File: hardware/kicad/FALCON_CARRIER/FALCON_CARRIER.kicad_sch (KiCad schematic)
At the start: 37 parts, among them J1 POWER_INPUT, J10 LEAK_SENSOR_TBD, J11 FAN_TBD, J12 SERVICE_I2C, J2 BAR02_I2C, J3 GPS_UART, J4 INA260_BAT_LOGIC, J5 INA260_SOLAR_0X41, J6 MCP9808_0X18, J7 ANEMOMETER, J8 WIND_VANE, J9 DS18B20_OPTION, U1 REGULATOR_3V3_TBD, U2 ESP32_DEVKITC_V4_WROOM32E, U3 BNO085_SPI, U4 ADS1115_0X48, U5 FAN_DRIVER_TBD

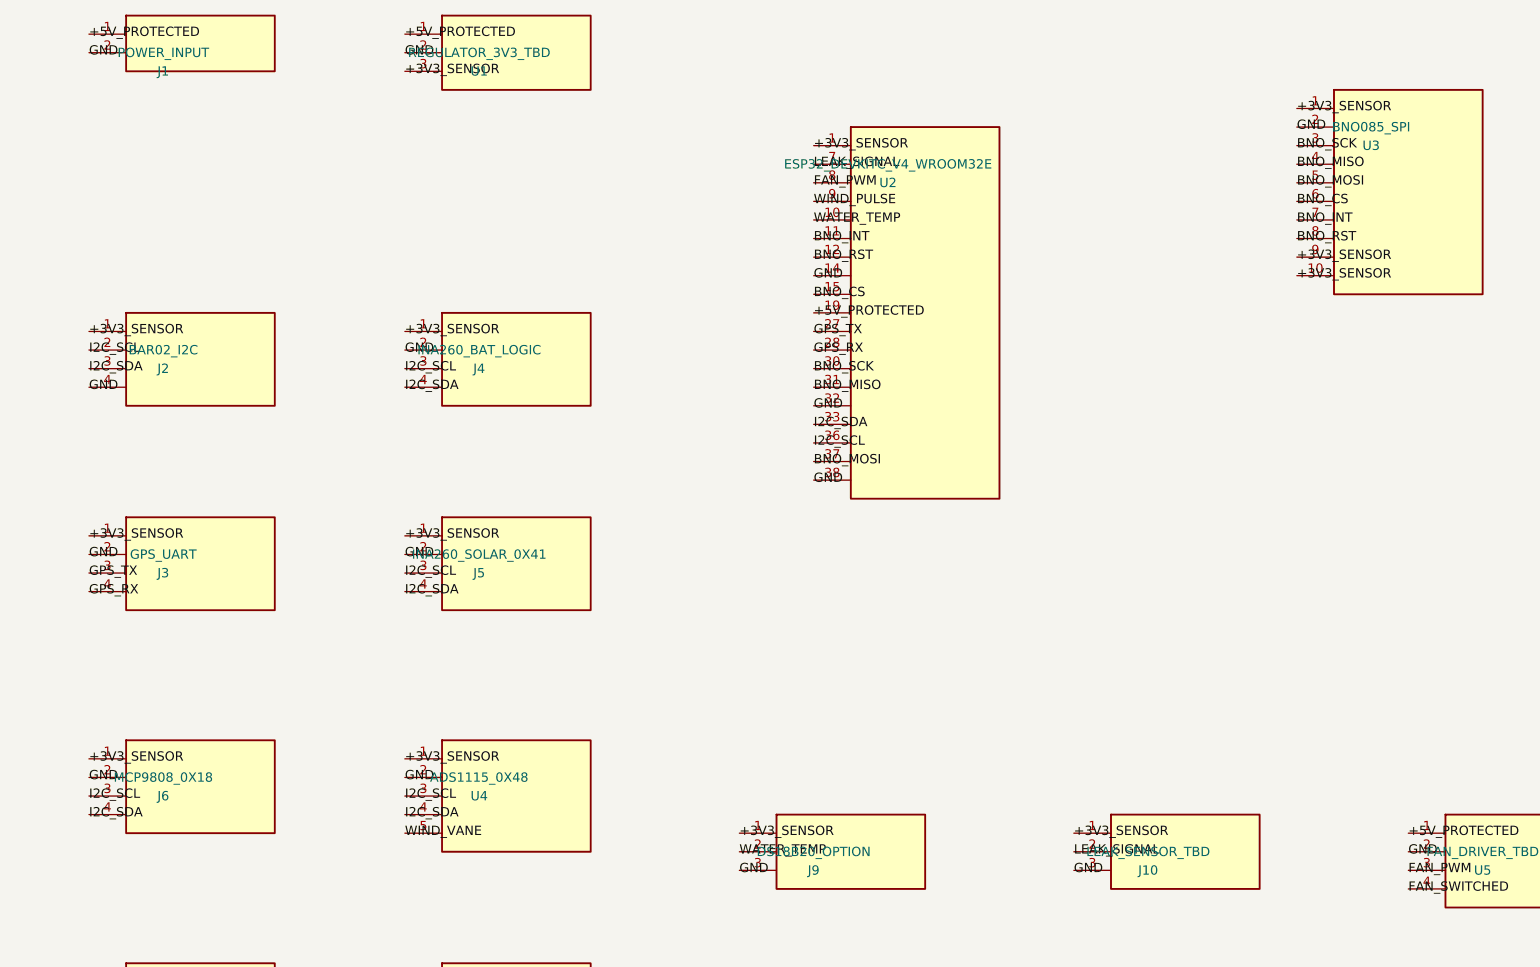
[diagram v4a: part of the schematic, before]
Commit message: Replace provisional carrier modules with official CAD footprints
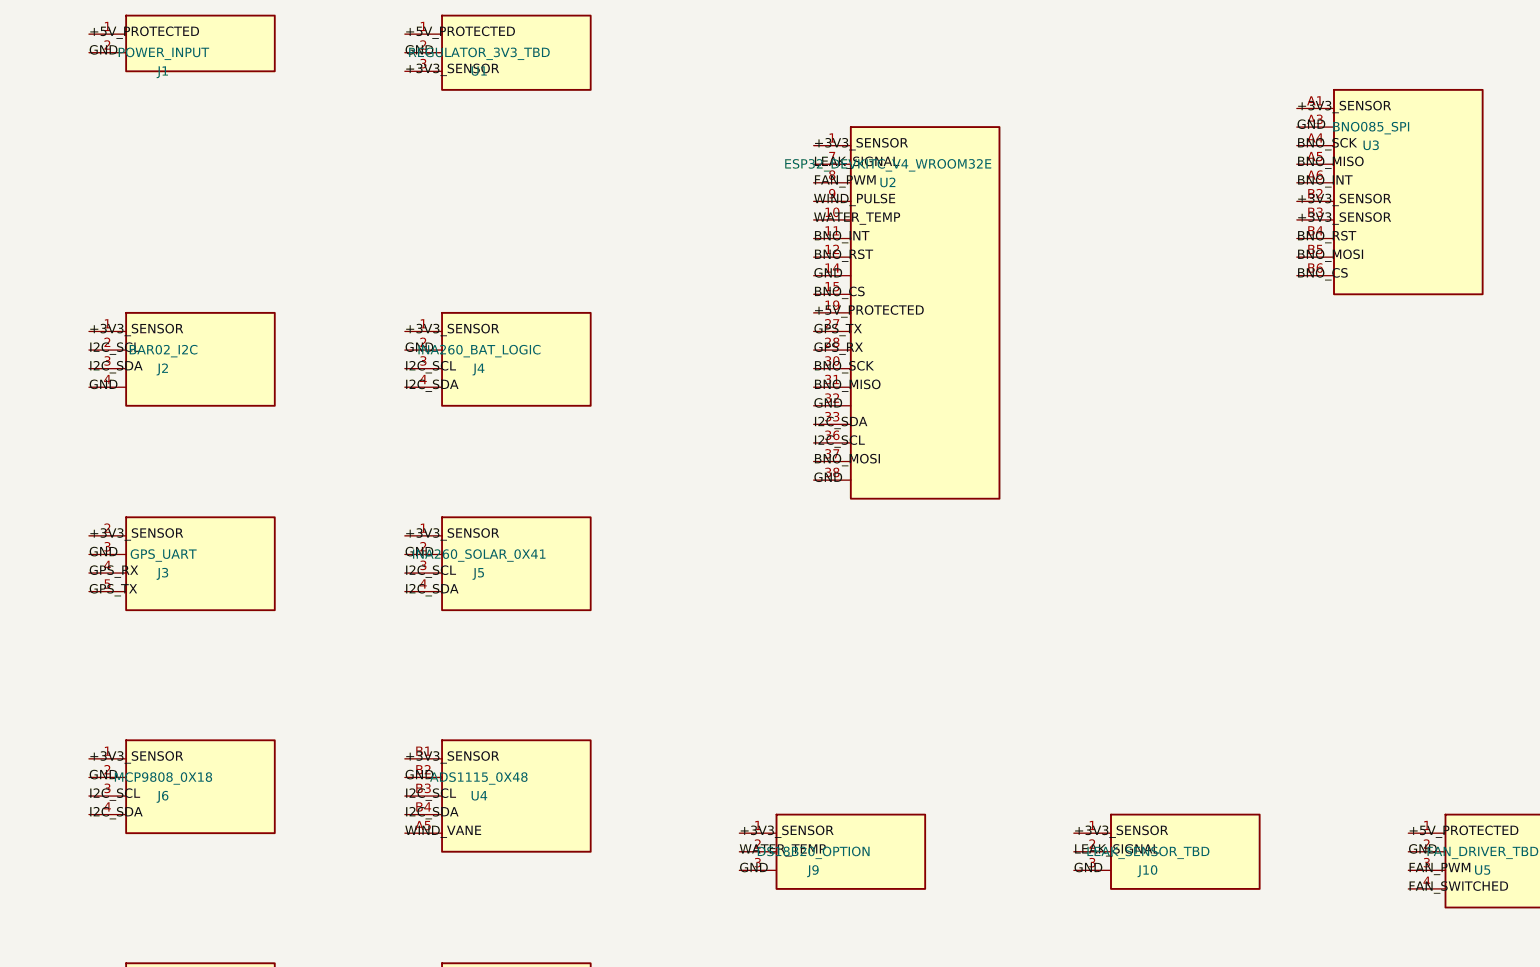
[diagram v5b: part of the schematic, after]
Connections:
- net +3V3_SENSOR: now also J3.2 (+3V3_SENSOR), U3.A1 (+3V3_SENSOR), U3.B2 (+3V3_SENSOR), U3.B3 (+3V3_SENSOR), U4.B1 (+3V3_SENSOR); no longer J3.1 (+3V3_SENSOR), U3.1 (+3V3_SENSOR), U3.10 (+3V3_SENSOR), U3.9 (+3V3_SENSOR), U4.1 (+3V3_SENSOR)
- net BNO_CS: now also U3.B6 (BNO_CS); no longer U3.6 (BNO_CS)
- net BNO_INT: now also U3.A6 (BNO_INT); no longer U3.7 (BNO_INT)
- net BNO_MISO: now also U3.A5 (BNO_MISO); no longer U3.4 (BNO_MISO)
- net BNO_MOSI: now also U3.B5 (BNO_MOSI); no longer U3.5 (BNO_MOSI)
- net BNO_RST: now also U3.B4 (BNO_RST); no longer U3.8 (BNO_RST)
- net BNO_SCK: now also U3.A4 (BNO_SCK); no longer U3.3 (BNO_SCK)
- net GND: now also J3.3 (GND), U3.A3 (GND), U4.B2 (GND); no longer J3.2 (GND), U3.2 (GND), U4.2 (GND)
- net GPS_TX: now also J3.5 (GPS_TX); no longer J3.3 (GPS_TX)
- net I2C_SCL: now also U4.B3 (I2C_SCL); no longer U4.3 (I2C_SCL)
- net I2C_SDA: now also U4.B4 (I2C_SDA); no longer U4.4 (I2C_SDA)
- net WIND_VANE: now also U4.A5 (WIND_VANE); no longer U4.5 (WIND_VANE)
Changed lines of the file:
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@@
   (label "BNO_MISO" (at 210.82 53.34 0)
     (effects (font (size 1.27 1.27))))
-  (label "BNO_MOSI" (at 210.82 55.88 0)
-    (effects (font (size 1.27 1.27))))
-  (label "BNO_CS" (at 210.82 58.42 0)
-    (effects (font (size 1.27 1.27))))
-  (label "BNO_INT" (at 210.82 60.96 0)
+  (label "BNO_INT" (at 210.82 55.88 0)
+    (effects (font (size 1.27 1.27))))
+  (label "+3V3_SENSOR" (at 210.82 58.42 0)
+    (effects (font (size 1.27 1.27))))
+  (label "+3V3_SENSOR" (at 210.82 60.96 0)
     (effects (font (size 1.27 1.27))))
   (label "BNO_RST" (at 210.82 63.50 0)
     (effects (font (size 1.27 1.27))))
-  (label "+3V3_SENSOR" (at 210.82 66.04 0)
-    (effects (font (size 1.27 1.27))))
-  (label "+3V3_SENSOR" (at 210.82 68.58 0)
+  (label "BNO_MOSI" (at 210.82 66.04 0)
+    (effects (font (size 1.27 1.27))))
+  (label "BNO_CS" (at 210.82 68.58 0)
     (effects (font (size 1.27 1.27))))
   (label "+3V3_SENSOR" (at 45.72 76.20 0)
@@
   (label "GND" (at 45.72 106.68 0)
     (effects (font (size 1.27 1.27))))
-  (label "GPS_TX" (at 45.72 109.22 0)
-    (effects (font (size 1.27 1.27))))
-  (label "GPS_RX" (at 45.72 111.76 0)
+  (label "GPS_RX" (at 45.72 109.22 0)
+    (effects (font (size 1.27 1.27))))
+  (label "GPS_TX" (at 45.72 111.76 0)
     (effects (font (size 1.27 1.27))))
   (label "+3V3_SENSOR" (at 88.90 76.20 0)
@@
     (property "Datasheet" "" (at 220.98 45.72 0) (effects (font (size 1.27 1.27)) (hide yes)))
     (property "Description" "FALCON carrier placeholder; footprint TBD" (at 220.98 45.72 0) (effects (font (size 1.27 1.27)) (hide yes)))
-    (pin "1")
-    (pin "2")
-    (pin "3")
-    (pin "4")
-    (pin "5")
-    (pin "6")
-    (pin "7")
-    (pin "8")
-    (pin "9")
-    (pin "10")
+    (pin "A1")
+    (pin "A3")
+    (pin "A4")
+    (pin "A5")
+    (pin "A6")
+    (pin "B2")
+    (pin "B3")
+    (pin "B4")
+    (pin "B5")
+    (pin "B6")
     (instances (project "FALCON_CARRIER"
       (path "/8f84bda8-4a60-4fb6-9df1-43d0356dc759" (reference "U3") (unit 1))))
@@
     (property "Datasheet" "" (at 55.88 104.14 0) (effects (font (size 1.27 1.27)) (hide yes)))
     (property "Description" "FALCON carrier placeholder; footprint TBD" (at 55.88 104.14 0) (effects (font (size 1.27 1.27)) (hide yes)))
-    (pin "1")
-    (pin "2")
-    (pin "3")
-    (pin "4")
+    (pin "2")
+    (pin "3")
+    (pin "4")
+    (pin "5")
     (instances (project "FALCON_CARRIER"
       (path "/8f84bda8-4a60-4fb6-9df1-43d0356dc759" (reference "J3") (unit 1))))
@@
     (property "Datasheet" "" (at 99.06 134.62 0) (effects (font (size 1.27 1.27)) (hide yes)))
     (property "Description" "FALCON carrier placeholder; footprint TBD" (at 99.06 134.62 0) (effects (font (size 1.27 1.27)) (hide yes)))
-    (pin "1")
-    (pin "2")
-    (pin "3")
-    (pin "4")
-    (pin "5")
+    (pin "B1")
+    (pin "B2")
+    (pin "B3")
+    (pin "B4")
+    (pin "A5")
     (instances (project "FALCON_CARRIER"
       (path "/8f84bda8-4a60-4fb6-9df1-43d0356dc759" (reference "U4") (unit 1))))

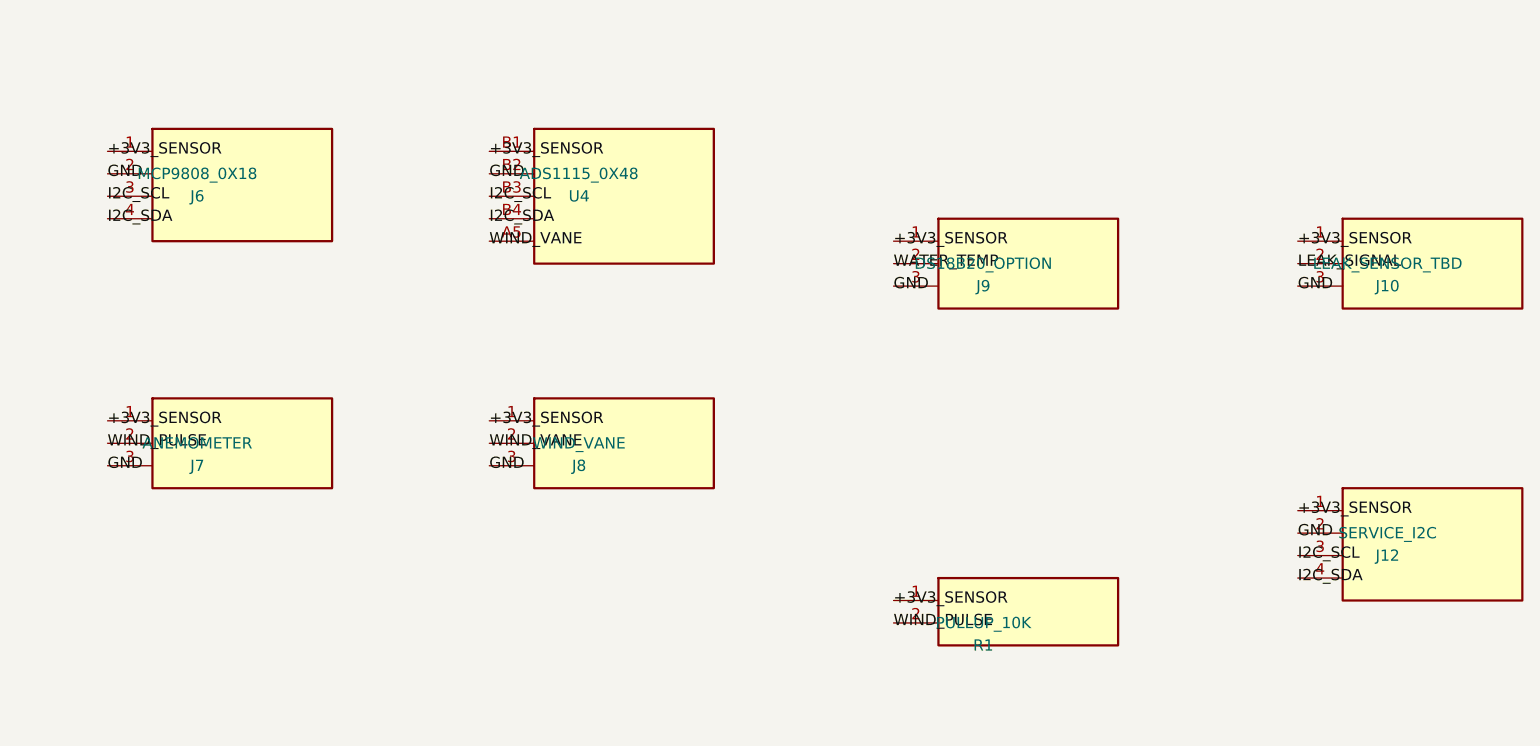
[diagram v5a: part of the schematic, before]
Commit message: Select keyed carrier connector families
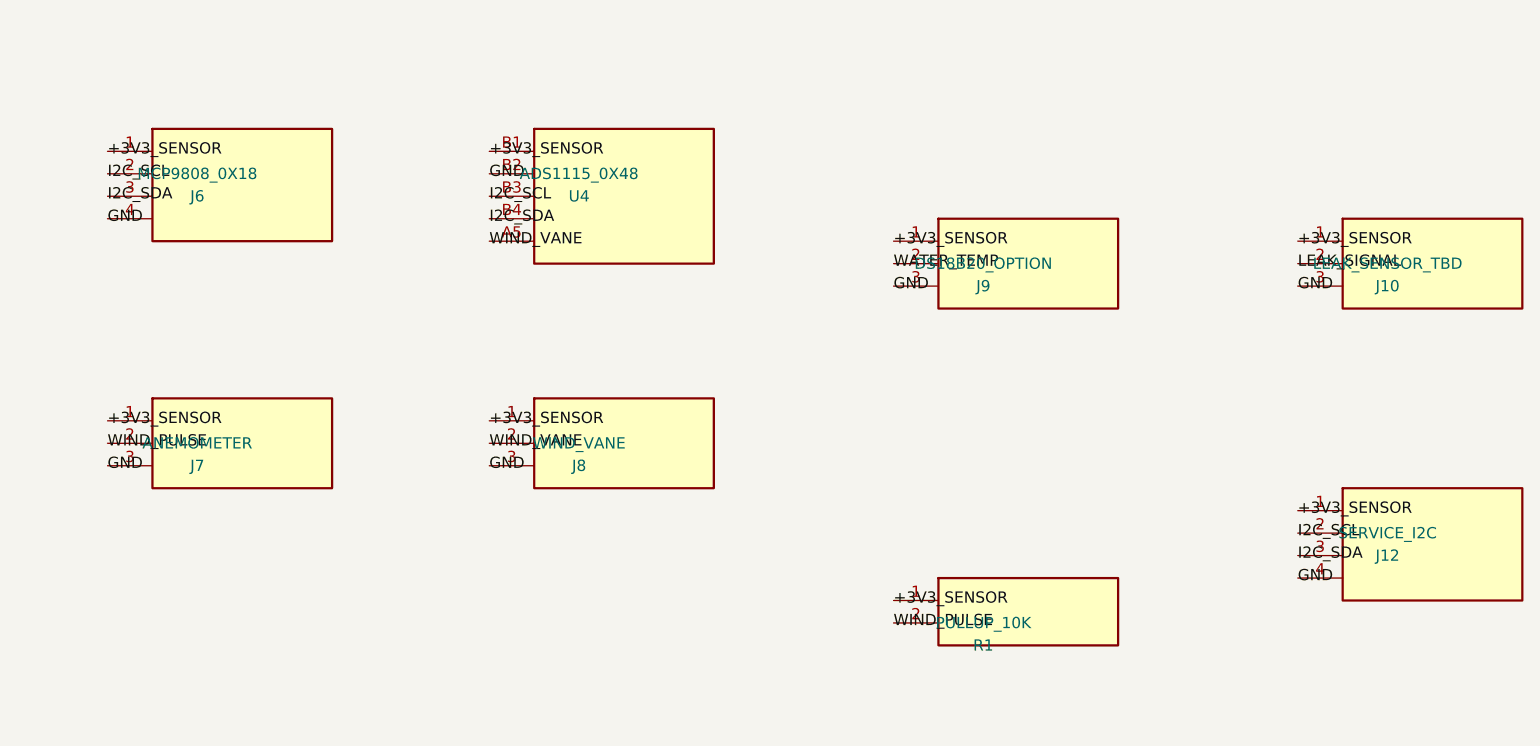
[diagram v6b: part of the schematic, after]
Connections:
- net GND: now also J12.4 (GND), J6.4 (GND); no longer J12.2 (GND), J6.2 (GND)
- net I2C_SCL: now also J12.2 (I2C_SCL), J6.2 (I2C_SCL); no longer J12.3 (I2C_SCL), J6.3 (I2C_SCL)
- net I2C_SDA: now also J12.3 (I2C_SDA), J6.3 (I2C_SDA); no longer J12.4 (I2C_SDA), J6.4 (I2C_SDA)
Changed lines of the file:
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@@
   (label "+3V3_SENSOR" (at 45.72 134.62 0)
     (effects (font (size 1.27 1.27))))
-  (label "GND" (at 45.72 137.16 0)
+  (label "I2C_SCL" (at 45.72 137.16 0)
     (effects (font (size 1.27 1.27))))
-  (label "I2C_SCL" (at 45.72 139.70 0)
+  (label "I2C_SDA" (at 45.72 139.70 0)
     (effects (font (size 1.27 1.27))))
-  (label "I2C_SDA" (at 45.72 142.24 0)
+  (label "GND" (at 45.72 142.24 0)
     (effects (font (size 1.27 1.27))))
   (label "+3V3_SENSOR" (at 88.90 134.62 0)
@@
   (label "+3V3_SENSOR" (at 180.34 175.26 0)
     (effects (font (size 1.27 1.27))))
-  (label "GND" (at 180.34 177.80 0)
+  (label "I2C_SCL" (at 180.34 177.80 0)
     (effects (font (size 1.27 1.27))))
-  (label "I2C_SCL" (at 180.34 180.34 0)
+  (label "I2C_SDA" (at 180.34 180.34 0)
     (effects (font (size 1.27 1.27))))
-  (label "I2C_SDA" (at 180.34 182.88 0)
+  (label "GND" (at 180.34 182.88 0)
     (effects (font (size 1.27 1.27))))
   (label "+3V3_SENSOR" (at 134.62 185.42 0)

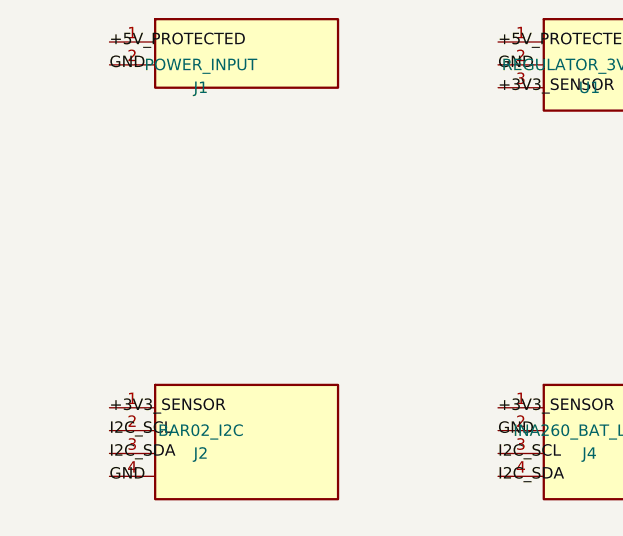
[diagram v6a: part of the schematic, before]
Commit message: Add protected 5V source interlock baseline
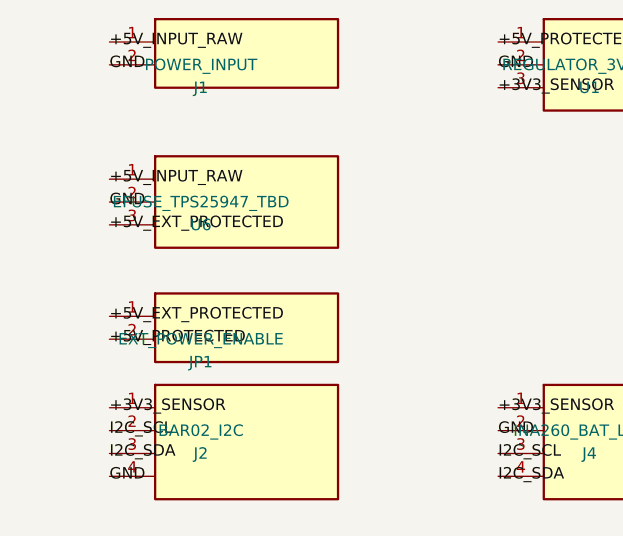
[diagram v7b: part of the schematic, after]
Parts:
- added JP1: EXT_POWER_ENABLE, symbol FALCON:EXT_POWER_ENABLE
- added U6: EFUSE_TPS25947_TBD, symbol FALCON:EFUSE_TPS25947_TBD
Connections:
- net +5V_PROTECTED: now also JP1.2 (+5V_PROTECTED); no longer J1.1 (+5V_PROTECTED)
- net GND: now also U6.2 (GND)
- new net +5V_EXT_PROTECTED: JP1.1 (+5V_EXT_PROTECTED), U6.3 (+5V_EXT_PROTECTED)
- new net +5V_INPUT_RAW: J1.1 (+5V_INPUT_RAW), U6.1 (+5V_INPUT_RAW)
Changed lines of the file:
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@@
     (comment 1 "NOT APPROVED FOR FABRICATION")
     (comment 2 "Named-net module schematic; footprints and protection values require physical validation"))
-  (label "+5V_PROTECTED" (at 45.72 35.56 0)
+  (label "+5V_INPUT_RAW" (at 45.72 35.56 0)
     (effects (font (size 1.27 1.27))))
   (label "GND" (at 45.72 38.10 0)
+    (effects (font (size 1.27 1.27))))
+  (label "+5V_INPUT_RAW" (at 45.72 50.80 0)
+    (effects (font (size 1.27 1.27))))
+  (label "GND" (at 45.72 53.34 0)
+    (effects (font (size 1.27 1.27))))
+  (label "+5V_EXT_PROTECTED" (at 45.72 55.88 0)
+    (effects (font (size 1.27 1.27))))
+  (label "+5V_EXT_PROTECTED" (at 45.72 66.04 0)
+    (effects (font (size 1.27 1.27))))
+  (label "+5V_PROTECTED" (at 45.72 68.58 0)
     (effects (font (size 1.27 1.27))))
   (label "+5V_PROTECTED" (at 88.90 35.56 0)
@@
   )
   (symbol
+    (lib_id "FALCON:EFUSE_TPS25947_TBD") (at 55.88 50.80 0) (unit 1)
+    (exclude_from_sim no) (in_bom yes) (on_board yes) (dnp no)
+    (property "Reference" "U6" (at 55.88 55.88 0) (effects (font (size 1.27 1.27))))
+    (property "Value" "EFUSE_TPS25947_TBD" (at 55.88 53.34 0) (effects (font (size 1.27 1.27))))
+    (property "Footprint" "" (at 55.88 50.80 0) (effects (font (size 1.27 1.27)) (hide yes)))
+    (property "Datasheet" "" (at 55.88 50.80 0) (effects (font (size 1.27 1.27)) (hide yes)))
+    (property "Description" "FALCON carrier placeholder; footprint TBD" (at 55.88 50.80 0) (effects (font (size 1.27 1.27)) (hide yes)))
+    (pin "1")
+    (pin "2")
+    (pin "3")
+    (instances (project "FALCON_CARRIER"
+      (path "/8f84bda8-4a60-4fb6-9df1-43d0356dc759" (reference "U6") (unit 1))))
+  )
+  (symbol
+    (lib_id "FALCON:EXT_POWER_ENABLE") (at 55.88 66.04 0) (unit 1)
+    (exclude_from_sim no) (in_bom yes) (on_board yes) (dnp no)
+    (property "Reference" "JP1" (at 55.88 71.12 0) (effects (font (size 1.27 1.27))))
+    (property "Value" "EXT_POWER_ENABLE" (at 55.88 68.58 0) (effects (font (size 1.27 1.27))))
+    (property "Footprint" "" (at 55.88 66.04 0) (effects (font (size 1.27 1.27)) (hide yes)))
+    (property "Datasheet" "" (at 55.88 66.04 0) (effects (font (size 1.27 1.27)) (hide yes)))
+    (property "Description" "FALCON carrier placeholder; footprint TBD" (at 55.88 66.04 0) (effects (font (size 1.27 1.27)) (hide yes)))
+    (pin "1")
+    (pin "2")
+    (instances (project "FALCON_CARRIER"
+      (path "/8f84bda8-4a60-4fb6-9df1-43d0356dc759" (reference "JP1") (unit 1))))
+  )
+  (symbol
